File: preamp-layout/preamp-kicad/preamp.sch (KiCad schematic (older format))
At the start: 13 parts, among them P1 Conn_WallPlug, SW1 Rotary_Encoder_Switch, SW10 SW_Push_Open, SW11 SW_Push_Open, SW2 Rotary_Encoder_Switch, SW3 SW_SPST, SW4 SW_Push_Open, SW5 SW_Push_Open, SW6 SW_Push_Open, SW7 SW_Push_Open, SW8 SW_Push_Open, SW9 SW_Push_Open

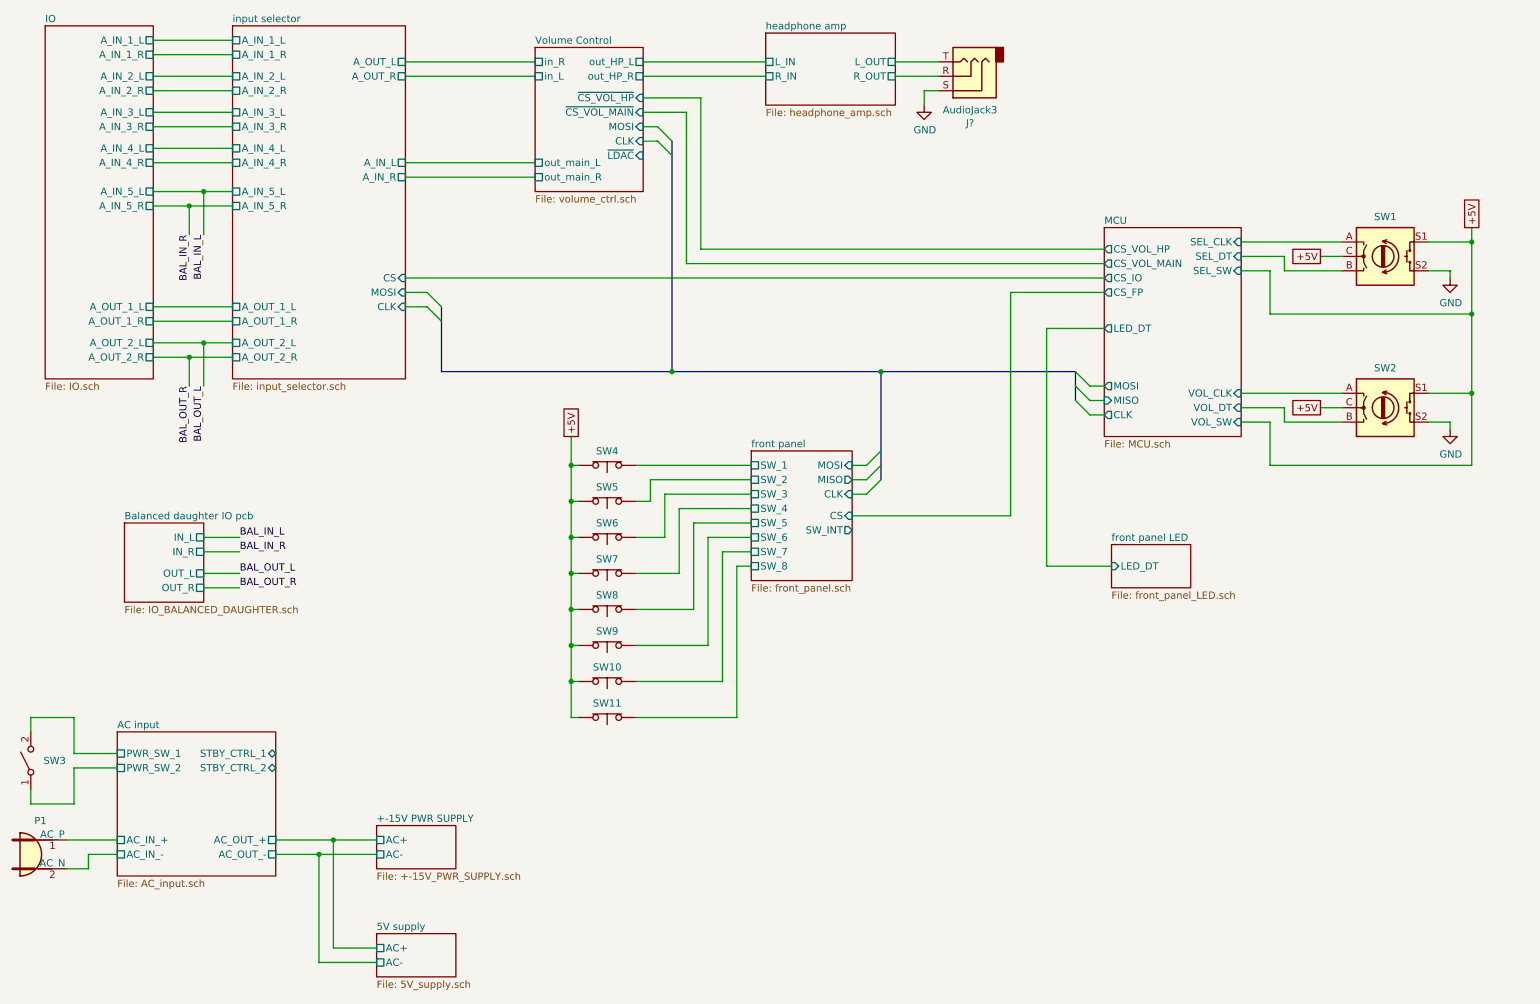
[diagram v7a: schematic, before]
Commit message: BOM Update
parts added to BOM, connector cleanup. Stopping point before renumbering refdes in a more intelligent way.
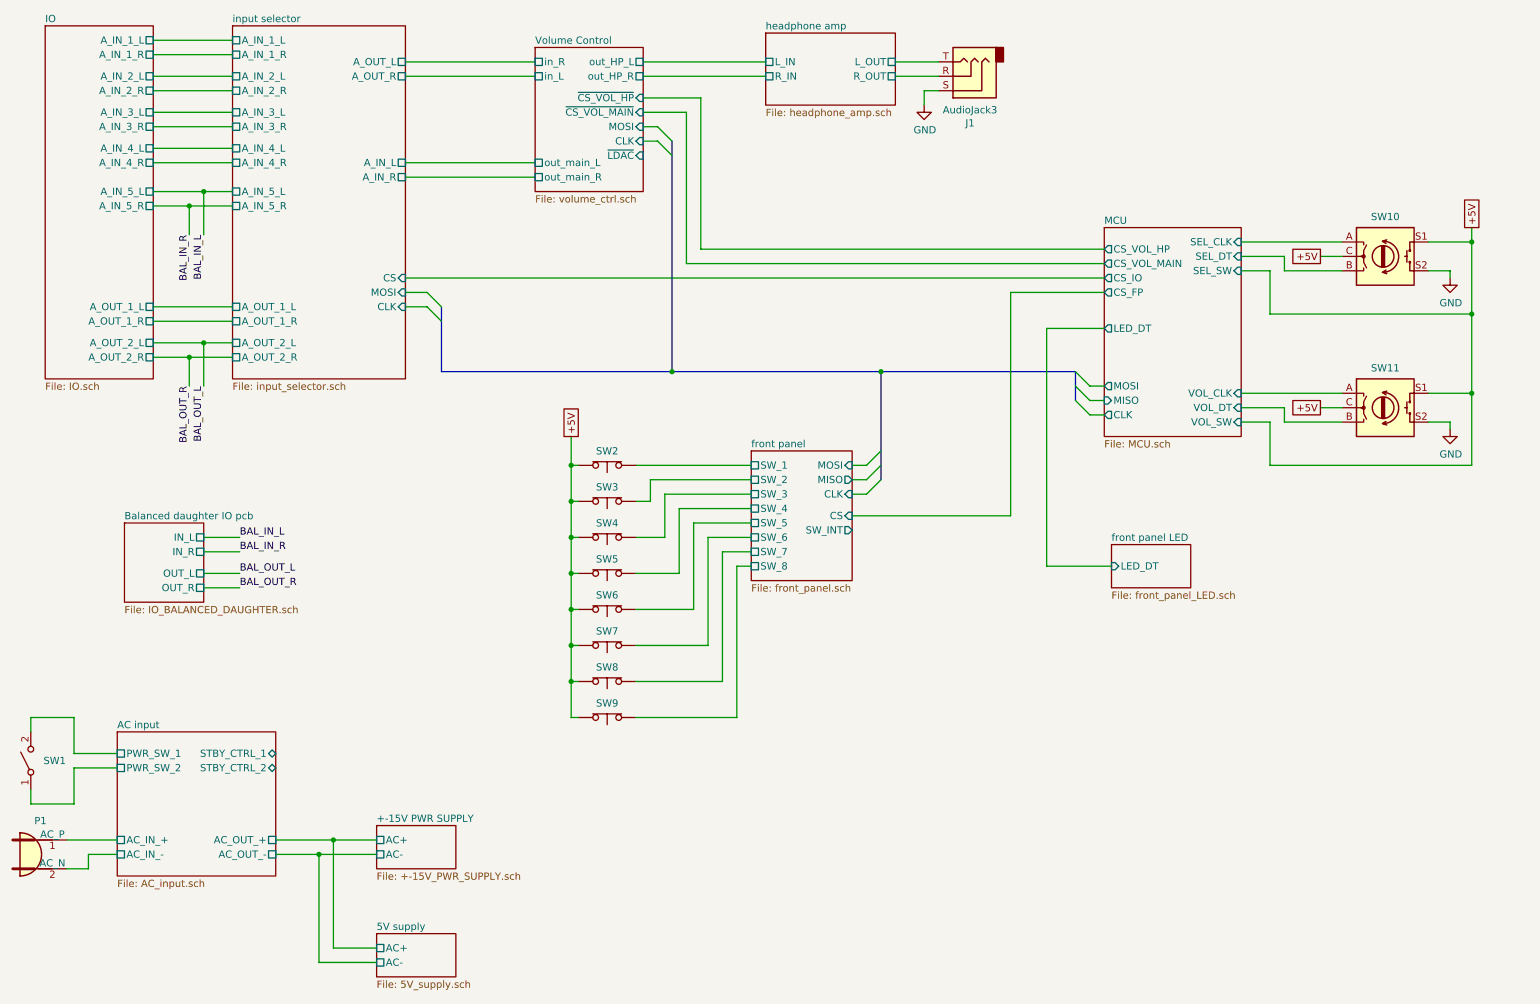
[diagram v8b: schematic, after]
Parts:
- gave numbers to parts that had none: 1
- renumbered SW3 to SW1, SW1 to SW10, SW2 to SW11, SW4 to SW2, SW5 to SW3, SW6 to SW4, SW7 to SW5, SW8 to SW6, SW9 to SW7, SW10 to SW8, SW11 to SW9
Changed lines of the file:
@@
 P 10150 2500
 AR Path="/63AE120F/5E975BA4" Ref="SW?"  Part="1"
-AR Path="/5E975BA4" Ref="SW1"  Part="1"
-F 0 "SW1" H 10150 2775 50  0000 C CNN
+AR Path="/5E975BA4" Ref="SW10"  Part="1"
+F 0 "SW10" H 10150 2775 50  0000 C CNN
 F 1 "Rotary_Encoder_Switch" H 10150 2776 50  0001 C CNN
 F 2 "" H 10000 2660 50  0001 C CNN
@@
 P 10150 3550
 AR Path="/63AE120F/5E9C5C27" Ref="SW?"  Part="1"
-AR Path="/5E9C5C27" Ref="SW2"  Part="1"
-F 0 "SW2" H 10150 3825 50  0000 C CNN
+AR Path="/5E9C5C27" Ref="SW11"  Part="1"
+F 0 "SW11" H 10150 3825 50  0000 C CNN
 F 1 "Rotary_Encoder_Switch" H 10150 3826 50  0001 C CNN
 F 2 "" H 10000 3710 50  0001 C CNN
@@
 P 10600 3700
 AR Path="/5E26F6FE/64ECC6E1" Ref="#PWR?"  Part="1"
-AR Path="/64ECC6E1" Ref="#PWR02"  Part="1"
-F 0 "#PWR02" H 10600 3450 50  0001 C CNN
+AR Path="/64ECC6E1" Ref="#PWR03"  Part="1"
+F 0 "#PWR03" H 10600 3450 50  0001 C CNN
 F 1 "GND" H 10605 3527 50  0000 C CNN
 F 2 "" H 10600 3700 50  0001 C CNN
@@
 P 10600 2650
 AR Path="/5E26F6FE/64ED30B9" Ref="#PWR?"  Part="1"
-AR Path="/64ED30B9" Ref="#PWR01"  Part="1"
-F 0 "#PWR01" H 10600 2400 50  0001 C CNN
+AR Path="/64ED30B9" Ref="#PWR02"  Part="1"
+F 0 "#PWR02" H 10600 2400 50  0001 C CNN
 F 1 "GND" H 10605 2477 50  0000 C CNN
 F 2 "" H 10600 2650 50  0001 C CNN
@@
 P 750 6000
 AR Path="/5E26F6FE/5E2E8D21" Ref="SW?"  Part="1"
-AR Path="/5E2E8D21" Ref="SW3"  Part="1"
-F 0 "SW3" V 750 5912 50  0000 R CNN
+AR Path="/5E2E8D21" Ref="SW1"  Part="1"
+F 0 "SW1" V 750 5912 50  0000 R CNN
 F 1 "SW_SPST" H 750 6144 50  0001 C CNN
 F 2 "" H 750 6000 50  0001 C CNN
@@
 P 4750 4200
 AR Path="/5E5ECAAE/5ED81ED2" Ref="SW?"  Part="1"
-AR Path="/5ED81ED2" Ref="SW5"  Part="1"
-F 0 "SW5" H 4750 4101 50  0000 C CNN
+AR Path="/5ED81ED2" Ref="SW3"  Part="1"
+F 0 "SW3" H 4750 4101 50  0000 C CNN
 F 1 "SW_Push_Open" V 4795 4277 50  0001 L CNN
 F 2 "" H 4750 4400 50  0001 C CNN
@@
 P 4750 4450
 AR Path="/5E5ECAAE/5ED81ED9" Ref="SW?"  Part="1"
-AR Path="/5ED81ED9" Ref="SW6"  Part="1"
-F 0 "SW6" H 4750 4351 50  0000 C CNN
+AR Path="/5ED81ED9" Ref="SW4"  Part="1"
+F 0 "SW4" H 4750 4351 50  0000 C CNN
 F 1 "SW_Push_Open" V 4795 4527 50  0001 L CNN
 F 2 "" H 4750 4650 50  0001 C CNN
@@
 P 4750 4700
 AR Path="/5E5ECAAE/5ED81EE0" Ref="SW?"  Part="1"
-AR Path="/5ED81EE0" Ref="SW7"  Part="1"
-F 0 "SW7" H 4750 4601 50  0000 C CNN
+AR Path="/5ED81EE0" Ref="SW5"  Part="1"
+F 0 "SW5" H 4750 4601 50  0000 C CNN
 F 1 "SW_Push_Open" V 4795 4777 50  0001 L CNN
 F 2 "" H 4750 4900 50  0001 C CNN
@@
 P 4750 4950
 AR Path="/5E5ECAAE/5ED81EE7" Ref="SW?"  Part="1"
-AR Path="/5ED81EE7" Ref="SW8"  Part="1"
-F 0 "SW8" H 4750 4851 50  0000 C CNN
+AR Path="/5ED81EE7" Ref="SW6"  Part="1"
+F 0 "SW6" H 4750 4851 50  0000 C CNN
 F 1 "SW_Push_Open" V 4795 5027 50  0001 L CNN
 F 2 "" H 4750 5150 50  0001 C CNN
@@
 P 4750 3950
 AR Path="/5E5ECAAE/5ED81EF3" Ref="SW?"  Part="1"
-AR Path="/5ED81EF3" Ref="SW4"  Part="1"
-F 0 "SW4" H 4750 3851 50  0000 C CNN
+AR Path="/5ED81EF3" Ref="SW2"  Part="1"
+F 0 "SW2" H 4750 3851 50  0000 C CNN
 F 1 "SW_Push_Open" V 4795 4027 50  0001 L CNN
 F 2 "" H 4750 4150 50  0001 C CNN
@@
 P 4750 5700
 AR Path="/5E5ECAAE/5ED81EFB" Ref="SW?"  Part="1"
-AR Path="/5ED81EFB" Ref="SW11"  Part="1"
-F 0 "SW11" H 4750 5601 50  0000 C CNN
+AR Path="/5ED81EFB" Ref="SW9"  Part="1"
+F 0 "SW9" H 4750 5601 50  0000 C CNN
 F 1 "SW_Push_Open" V 4795 5777 50  0001 L CNN
 F 2 "" H 4750 5900 50  0001 C CNN
@@
 P 4750 5450
 AR Path="/5E5ECAAE/5ED81F03" Ref="SW?"  Part="1"
-AR Path="/5ED81F03" Ref="SW10"  Part="1"
-F 0 "SW10" H 4750 5351 50  0000 C CNN
+AR Path="/5ED81F03" Ref="SW8"  Part="1"
+F 0 "SW8" H 4750 5351 50  0000 C CNN
 F 1 "SW_Push_Open" V 4795 5527 50  0001 L CNN
 F 2 "" H 4750 5650 50  0001 C CNN
@@
 P 4750 5200
 AR Path="/5E5ECAAE/5ED81F0B" Ref="SW?"  Part="1"
-AR Path="/5ED81F0B" Ref="SW9"  Part="1"
-F 0 "SW9" H 4750 5101 50  0000 C CNN
+AR Path="/5ED81F0B" Ref="SW7"  Part="1"
+F 0 "SW7" H 4750 5101 50  0000 C CNN
 F 1 "SW_Push_Open" V 4795 5277 50  0001 L CNN
 F 2 "" H 4750 5400 50  0001 C CNN
@@
 P 7250 1250
 AR Path="/5E4A803E/5F4B3F32" Ref="J?"  Part="1"
-AR Path="/5F4B3F32" Ref="J?"  Part="1"
-F 0 "J?" H 7232 1575 50  0000 C CNN
+AR Path="/5F4B3F32" Ref="J1"  Part="1"
+F 0 "J1" H 7232 1575 50  0000 C CNN
 F 1 "AudioJack3" H 7232 1484 50  0000 C CNN
 F 2 "" H 7250 1250 50  0001 C CNN
@@
 AR Path="/6009D432/5F4B3F39" Ref="#PWR?"  Part="1"
 AR Path="/5E4A803E/5F4B3F39" Ref="#PWR?"  Part="1"
-AR Path="/5F4B3F39" Ref="#PWR?"  Part="1"
-F 0 "#PWR?" H 6950 1200 50  0001 C CNN
+AR Path="/5F4B3F39" Ref="#PWR01"  Part="1"
+F 0 "#PWR01" H 6950 1200 50  0001 C CNN
 F 1 "GND" H 6955 1277 50  0000 C CNN
 F 2 "" H 6950 1450 50  0001 C CNN
